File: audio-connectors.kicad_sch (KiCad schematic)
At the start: 0 parts

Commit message: almost done with clocking, need series terminators
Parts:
- added J1, J2: AudioJack2_Ground, Connector_Audio:Jack_3.5mm_CUI_SJ-3523-SMT_Horizontal, symbol Connector_Audio:AudioJack2_Ground
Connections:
- new net GND: J1.G, J2.G

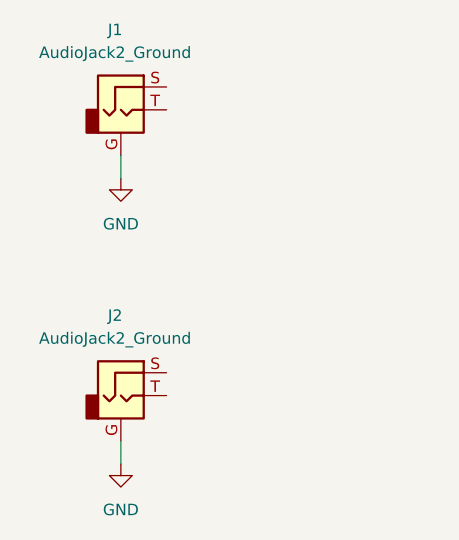
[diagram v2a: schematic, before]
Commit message: mostly done with schematic of mikrobus board
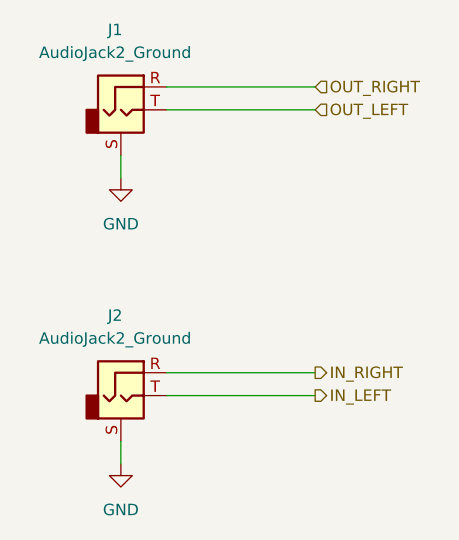
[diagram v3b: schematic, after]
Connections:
- net GND: now also J1.S, J2.S; no longer J1.G, J2.G
- net IN_LEFT: now reaches J2.T
- net OUT_LEFT: now reaches J1.T
- new net IN_RIGHT: J2.R
- new net OUT_RIGHT: J1.R
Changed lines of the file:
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@@
+	(wire
+		(pts
+			(xy 60.96 66.04) (xy 77.47 66.04)
+		)
+		(stroke
+			(width 0)
+			(type default)
+		)
+	)
 	(wire
 		(pts
@@
 	(wire
 		(pts
+			(xy 60.96 97.79) (xy 77.47 97.79)
+		)
+		(stroke
+			(width 0)
+			(type default)
+		)
+	)
+	(wire
+		(pts
 			(xy 55.88 71.12) (xy 55.88 73.66)
 		)
@@
 			(width 0)
 			(type default)
+		)
+	)
+	(wire
+		(pts
+			(xy 60.96 63.5) (xy 77.47 63.5)
+		)
+		(stroke
+			(width 0)
+			(type default)
+		)
+	)
+	(wire
+		(pts
+			(xy 60.96 95.25) (xy 77.47 95.25)
+		)
+		(stroke
+			(width 0)
+			(type default)
+		)
+	)
+	(hierarchical_label "OUT_LEFT"
+		(shape input)
+		(at 77.47 66.04 0)
+		(fields_autoplaced yes)
+		(effects
+			(font
+				(size 1.27 1.27)
+			)
+			(justify left)
+		)
+	)
+	(hierarchical_label "OUT_RIGHT"
+		(shape input)
+		(at 77.47 63.5 0)
+		(fields_autoplaced yes)
+		(effects
+			(font
+				(size 1.27 1.27)
+			)
+			(justify left)
+		)
+	)
+	(hierarchical_label "IN_LEFT"
+		(shape output)
+		(at 77.47 97.79 0)
+		(fields_autoplaced yes)
+		(effects
+			(font
+				(size 1.27 1.27)
+			)
+			(justify left)
+		)
+	)
+	(hierarchical_label "IN_RIGHT"
+		(shape output)
+		(at 77.47 95.25 0)
+		(fields_autoplaced yes)
+		(effects
+			(font
+				(size 1.27 1.27)
+			)
+			(justify left)
 		)
 	)
@@
 			)
 		)
-		(pin "G"
+		(pin "R"
 		)
 		(pin "T"
@@
 	)
 	(symbol
+		(lib_name "AudioJack2_Ground_1")
 		(lib_id "Connector_Audio:AudioJack2_Ground")
 		(at 55.88 66.04 0)
@@
 			)
 		)
-		(pin "G"
+		(pin "R"
 		)
 		(pin "T"
